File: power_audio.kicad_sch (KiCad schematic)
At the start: 3 parts, among them J1 Conn_01x03, J2 Conn_01x03, J5 Conn_01x02

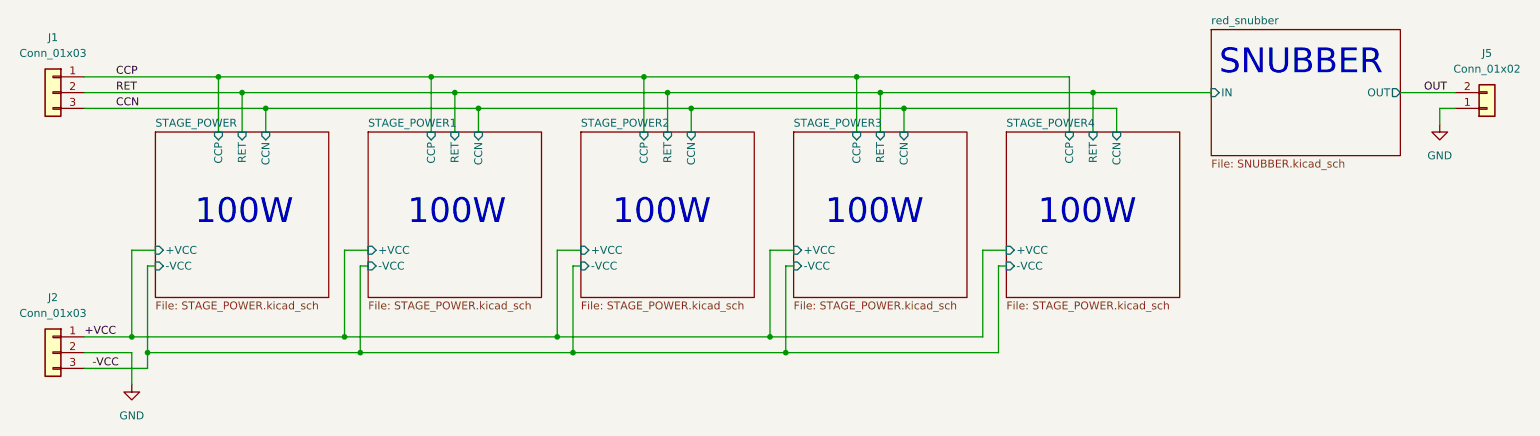
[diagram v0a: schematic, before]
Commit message: mejorando pistas
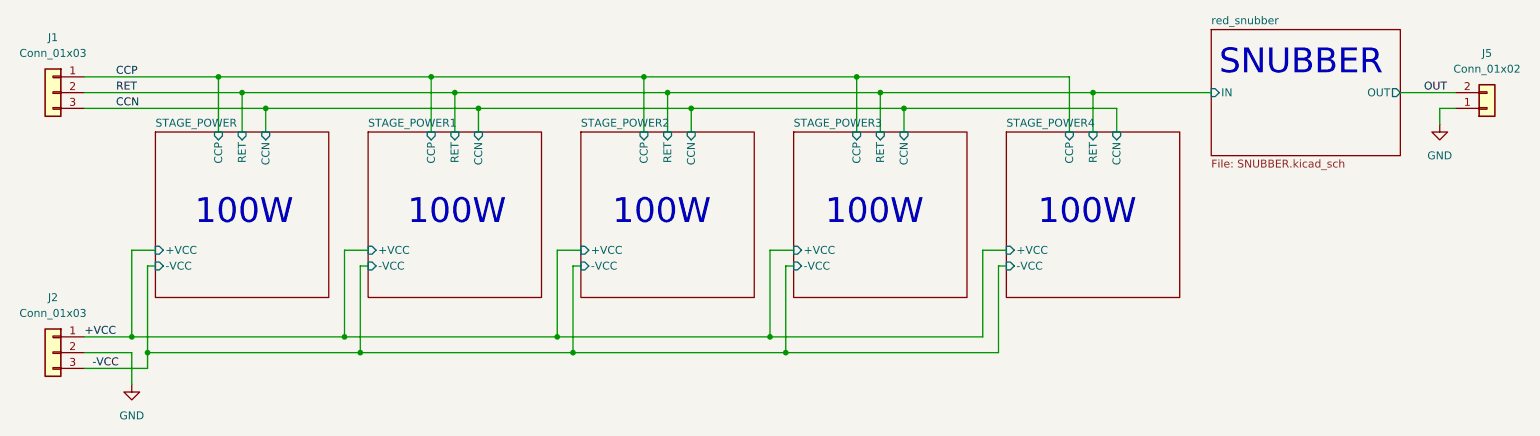
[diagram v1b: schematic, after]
